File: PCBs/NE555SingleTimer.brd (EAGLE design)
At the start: 24.2 x 19 mm, 7 parts, among them T1 2N3904

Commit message: Renamed files .
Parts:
- removed GND, INPUT, OUTPUT: MICROBIT_PAD, microbit:MICROBIT_PAD
- removed LED1: (no value), led:CHIP-LED0805
- removed R1, R2: (no value), we-rcl:R0207/10
- removed T1: 2N3904, transistor:TO92
- added IC1: LM555N, linear:DIL08
- added U$1, U$2, U$3, U$4: MICROBIT_PAD, microbit:MICROBIT_PAD
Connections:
- removed net N$3: R1.2, T1.2
- net 5V: now also IC1.4, IC1.8, U$3.PAD; no longer INPUT.PAD, R1.1, R2.2
- net GND: now also IC1.1, U$4.PAD; no longer GND.PAD, T1.3
- net N$1: now also IC1.3, U$1.PAD; no longer LED1.A, R2.1
- net N$2: now also IC1.2, IC1.6, U$2.PAD; no longer LED1.C, OUTPUT.PAD, T1.1
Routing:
- net N$1: track 1.95 -> 13.8 mm
- net 5V: track 10.3 -> 20.4 mm
- net N$3: track 6.06 -> 0.00 mm
- net GND: track 10.3 -> 5.17 mm
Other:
- board size 24.2 x 19 mm -> 16.5 x 31.8 mm
- board text added: "555IC"

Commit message: Updated
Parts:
- moved U$1 0.30 mm to (12.0, 25.0)
- moved U$2 0.13 mm to (4.32, 24.9)
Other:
- board size 16.5 x 31.8 mm -> 22.5 x 32 mm
- board text added: "PinwheelRobotics"
- board text added: "care@pinwheel"
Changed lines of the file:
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@@
 <drawing>
 <settings>
-<setting alwaysvectorfont="no"/>
+<setting alwaysvectorfont="yes"/>
 <setting verticaltext="up"/>
 </settings>
-<grid distance="50" unitdist="mil" unit="mm" style="lines" multiple="1" display="yes" altdistance="5" altunitdist="mil" altunit="mm"/>
+<grid distance="0.5" unitdist="mm" unit="mm" style="lines" multiple="1" display="yes" altdistance="5" altunitdist="mil" altunit="mm"/>
 <layers>
 <layer number="1" name="Top" color="4" fill="1" visible="yes" active="yes"/>
@@
 <layer number="43" name="vRestrict" color="2" fill="10" visible="yes" active="yes"/>
 <layer number="44" name="Drills" color="7" fill="1" visible="no" active="yes"/>
-<layer number="45" name="Holes" color="7" fill="1" visible="no" active="yes"/>
+<layer number="45" name="Holes" color="7" fill="1" visible="yes" active="yes"/>
 <layer number="46" name="Milling" color="3" fill="1" visible="no" active="yes"/>
 <layer number="47" name="Measures" color="7" fill="1" visible="no" active="yes"/>
@@
 <plain>
 <text x="15.113" y="15.621" size="0.4064" layer="21" rot="R90">555IC</text>
-<wire x1="1.27" y1="0" x2="15.24" y2="0" width="0.1524" layer="20"/>
-<wire x1="15.24" y1="0" x2="16.51" y2="1.27" width="0.1524" layer="20" curve="90"/>
-<wire x1="16.51" y1="1.27" x2="16.51" y2="30.48" width="0.1524" layer="20"/>
-<wire x1="16.51" y1="30.48" x2="15.24" y2="31.75" width="0.1524" layer="20" curve="90"/>
-<wire x1="15.24" y1="31.75" x2="1.27" y2="31.75" width="0.1524" layer="20"/>
-<wire x1="1.27" y1="31.75" x2="0" y2="30.48" width="0.1524" layer="20" curve="90"/>
-<wire x1="0" y1="30.48" x2="0" y2="1.27" width="0.1524" layer="20"/>
-<wire x1="0" y1="1.27" x2="1.27" y2="0" width="0.1524" layer="20" curve="90"/>
+<wire x1="-3" y1="30.788903125" x2="-3" y2="0.998303125" width="0.1524" layer="20"/>
+<wire x1="-3" y1="0.998303125" x2="-2.001696875" y2="0" width="0.1524" layer="20" curve="90"/>
+<wire x1="-2.001696875" y1="0" x2="17.86581875" y2="0" width="0.1524" layer="20"/>
+<wire x1="17.86581875" y1="0" x2="19.5" y2="1.63418125" width="0.1524" layer="20" curve="90"/>
+<wire x1="19.5" y1="1.63418125" x2="19.5" y2="30.165390625" width="0.1524" layer="20"/>
+<wire x1="19.5" y1="30.165390625" x2="17.665390625" y2="32" width="0.1524" layer="20" curve="90"/>
+<wire x1="17.665390625" y1="32" x2="-1.788903125" y2="32" width="0.1524" layer="20"/>
+<wire x1="-1.788903125" y1="32" x2="-3" y2="30.788903125" width="0.1524" layer="20" curve="90"/>
+<hole x="-1" y="30" drill="3"/>
+<hole x="17.5" y="29.881" drill="3"/>
+<hole x="17.5" y="2" drill="3"/>
+<hole x="-1" y="2" drill="3"/>
+<text x="0" y="6" size="1.778" layer="21" rot="R90">PinwheelRobotics </text>
+<text x="18.5" y="25" size="1.778" layer="22" rot="MR270">care@pinwheel</text>
 </plain>
 <attributes>
@@
 <attribute name="VALUE" x="5.207" y="15.24" size="1.27" layer="27" ratio="10"/>
 </element>
-<element name="U$1" library="microbit" package="MICROBIT_PAD" value="MICROBIT_PAD" x="12.192" y="24.765" smashed="yes" rot="R180">
-<attribute name="NAME" x="15.367" y="19.685" size="1.27" layer="21" rot="R90"/>
+<element name="U$1" library="microbit" package="MICROBIT_PAD" value="MICROBIT_PAD" x="12" y="25" smashed="yes" rot="R180">
+<attribute name="NAME" x="15.175" y="19.92" size="1.27" layer="21" rot="R90"/>
 </element>
-<element name="U$2" library="microbit" package="MICROBIT_PAD" value="MICROBIT_PAD" x="4.318" y="24.765" smashed="yes" rot="R180">
-<attribute name="NAME" x="1.016" y="20.447" size="1.27" layer="21"/>
+<element name="U$2" library="microbit" package="MICROBIT_PAD" value="MICROBIT_PAD" x="4.318" y="24.892" smashed="yes" rot="R180">
+<attribute name="NAME" x="1.016" y="20.574" size="1.27" layer="21"/>
 </element>
 <element name="U$3" library="microbit" package="MICROBIT_PAD" value="MICROBIT_PAD" x="12.192" y="6.985" smashed="yes">
@@
 <wire x1="11.2268" y1="19.1516" x2="10.2362" y2="18.161" width="0.508" layer="16"/>
 <wire x1="11.2268" y1="24.1046" x2="11.2268" y2="19.1516" width="0.508" layer="16"/>
-<wire x1="11.8872" y1="24.765" x2="11.2268" y2="24.1046" width="0.508" layer="16"/>
+<wire x1="12" y1="24.8778" x2="11.2268" y2="24.1046" width="0.508" layer="16"/>
 <wire x1="10.2362" y1="12.2174" x2="10.033" y2="12.065" width="0.508" layer="16"/>
-<wire x1="11.8872" y1="24.765" x2="12.192" y2="24.765" width="0.508" layer="16"/>
+<wire x1="12" y1="24.8778" x2="12" y2="25" width="0.508" layer="16"/>
 </signal>
 <signal name="N$2">
@@
 <wire x1="7.5946" y1="12.2174" x2="7.493" y2="12.065" width="0.508" layer="16"/>
 <wire x1="9.906" y1="19.4818" x2="10.033" y2="19.685" width="0.508" layer="16"/>
-<wire x1="4.953" y1="24.765" x2="10.033" y2="19.685" width="0.508" layer="16"/>
-<wire x1="4.318" y1="24.765" x2="4.953" y2="24.765" width="0.508" layer="16"/>
+<wire x1="4.826" y1="24.892" x2="10.033" y2="19.685" width="0.508" layer="16"/>
+<wire x1="4.318" y1="24.892" x2="4.826" y2="24.892" width="0.508" layer="16"/>
 </signal>
 <signal name="GND">

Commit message: New Update
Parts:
- moved U$3 0.40 mm to (11.8, 7.11)
- moved U$1 0.25 mm to (11.7, 25.0)
- moved U$4 0.13 mm to (4.32, 7.11)
- moved U$2 0.13 mm to (4.32, 25.0)
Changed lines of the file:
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@@
 <drawing>
 <settings>
-<setting alwaysvectorfont="yes"/>
+<setting alwaysvectorfont="no"/>
 <setting verticaltext="up"/>
 </settings>
@@
 <wire x1="-1.788903125" y1="32" x2="-3" y2="30.788903125" width="0.1524" layer="20" curve="90"/>
 <hole x="-1" y="30" drill="3"/>
-<hole x="17.5" y="29.881" drill="3"/>
-<hole x="17.5" y="2" drill="3"/>
+<hole x="17" y="30" drill="3"/>
+<hole x="17" y="2" drill="3"/>
 <hole x="-1" y="2" drill="3"/>
 <text x="0" y="6" size="1.778" layer="21" rot="R90">PinwheelRobotics </text>
@@
 <attribute name="VALUE" x="5.207" y="15.24" size="1.27" layer="27" ratio="10"/>
 </element>
-<element name="U$1" library="microbit" package="MICROBIT_PAD" value="MICROBIT_PAD" x="12" y="25" smashed="yes" rot="R180">
-<attribute name="NAME" x="15.175" y="19.92" size="1.27" layer="21" rot="R90"/>
+<element name="U$1" library="microbit" package="MICROBIT_PAD" value="MICROBIT_PAD" x="11.746" y="25" smashed="yes" rot="R180">
+<attribute name="NAME" x="14.921" y="19.92" size="1.27" layer="21" rot="R90"/>
 </element>
-<element name="U$2" library="microbit" package="MICROBIT_PAD" value="MICROBIT_PAD" x="4.318" y="24.892" smashed="yes" rot="R180">
-<attribute name="NAME" x="1.016" y="20.574" size="1.27" layer="21"/>
+<element name="U$2" library="microbit" package="MICROBIT_PAD" value="MICROBIT_PAD" x="4.318" y="25.019" smashed="yes" rot="R180">
+<attribute name="NAME" x="1.016" y="20.701" size="1.27" layer="21"/>
 </element>
-<element name="U$3" library="microbit" package="MICROBIT_PAD" value="MICROBIT_PAD" x="12.192" y="6.985" smashed="yes">
-<attribute name="NAME" x="14.097" y="11.176" size="1.27" layer="21" rot="R270"/>
+<element name="U$3" library="microbit" package="MICROBIT_PAD" value="MICROBIT_PAD" x="11.811" y="7.112" smashed="yes">
+<attribute name="NAME" x="13.716" y="11.303" size="1.27" layer="21" rot="R270"/>
 </element>
-<element name="U$4" library="microbit" package="MICROBIT_PAD" value="MICROBIT_PAD" x="4.445" y="7.112" smashed="yes">
-<attribute name="NAME" x="1.143" y="12.319" size="1.27" layer="21" rot="R270"/>
+<element name="U$4" library="microbit" package="MICROBIT_PAD" value="MICROBIT_PAD" x="4.318" y="7.112" smashed="yes">
+<attribute name="NAME" x="1.016" y="12.319" size="1.27" layer="21" rot="R270"/>
 </element>
 </elements>
@@
 <wire x1="12.5476" y1="7.5946" x2="12.5476" y2="10.8966" width="0.508" layer="16"/>
 <wire x1="12.5476" y1="10.8966" x2="12.5476" y2="11.8872" width="0.508" layer="16"/>
-<wire x1="12.2428" y1="7.2898" x2="12.5476" y2="7.5946" width="0.508" layer="16"/>
+<wire x1="12.1158" y1="7.1628" x2="12.5476" y2="7.5946" width="0.508" layer="16"/>
 <wire x1="12.5476" y1="11.8872" x2="12.573" y2="12.065" width="0.508" layer="16"/>
-<wire x1="12.2428" y1="7.2898" x2="12.192" y2="6.985" width="0.508" layer="16"/>
+<wire x1="12.1158" y1="7.1628" x2="11.811" y2="7.112" width="0.508" layer="16"/>
 <wire x1="4.953" y1="13.8684" x2="4.953" y2="19.685" width="0.508" layer="16"/>
 <wire x1="6.2738" y1="12.5476" x2="4.953" y2="13.8684" width="0.508" layer="16"/>
@@
 <wire x1="11.2268" y1="19.1516" x2="10.2362" y2="18.161" width="0.508" layer="16"/>
 <wire x1="11.2268" y1="24.1046" x2="11.2268" y2="19.1516" width="0.508" layer="16"/>
-<wire x1="12" y1="24.8778" x2="11.2268" y2="24.1046" width="0.508" layer="16"/>
+<wire x1="11.746" y1="24.6238" x2="11.2268" y2="24.1046" width="0.508" layer="16"/>
 <wire x1="10.2362" y1="12.2174" x2="10.033" y2="12.065" width="0.508" layer="16"/>
-<wire x1="12" y1="24.8778" x2="12" y2="25" width="0.508" layer="16"/>
+<wire x1="11.746" y1="24.6238" x2="11.746" y2="25" width="0.508" layer="16"/>
 </signal>
 <signal name="N$2">
@@
 <wire x1="7.5946" y1="12.2174" x2="7.493" y2="12.065" width="0.508" layer="16"/>
 <wire x1="9.906" y1="19.4818" x2="10.033" y2="19.685" width="0.508" layer="16"/>
-<wire x1="4.826" y1="24.892" x2="10.033" y2="19.685" width="0.508" layer="16"/>
-<wire x1="4.318" y1="24.892" x2="4.826" y2="24.892" width="0.508" layer="16"/>
+<wire x1="4.699" y1="25.019" x2="10.033" y2="19.685" width="0.508" layer="16"/>
+<wire x1="4.318" y1="25.019" x2="4.699" y2="25.019" width="0.508" layer="16"/>
 </signal>
 <signal name="GND">
 <contactref element="IC1" pad="1"/>
 <contactref element="U$4" pad="PAD"/>
-<wire x1="4.953" y1="7.5946" x2="4.953" y2="12.065" width="0.508" layer="16"/>
-<wire x1="4.6228" y1="7.2644" x2="4.953" y2="7.5946" width="0.508" layer="16"/>
-<wire x1="4.6228" y1="7.2644" x2="4.445" y2="7.112" width="0.508" layer="16"/>
+<wire x1="4.953" y1="7.656284375" x2="4.953" y2="12.065" width="0.508" layer="16"/>
+<wire x1="4.953" y1="7.656284375" x2="4.318" y2="7.112" width="0.508" layer="16"/>
 </signal>
 </signals>

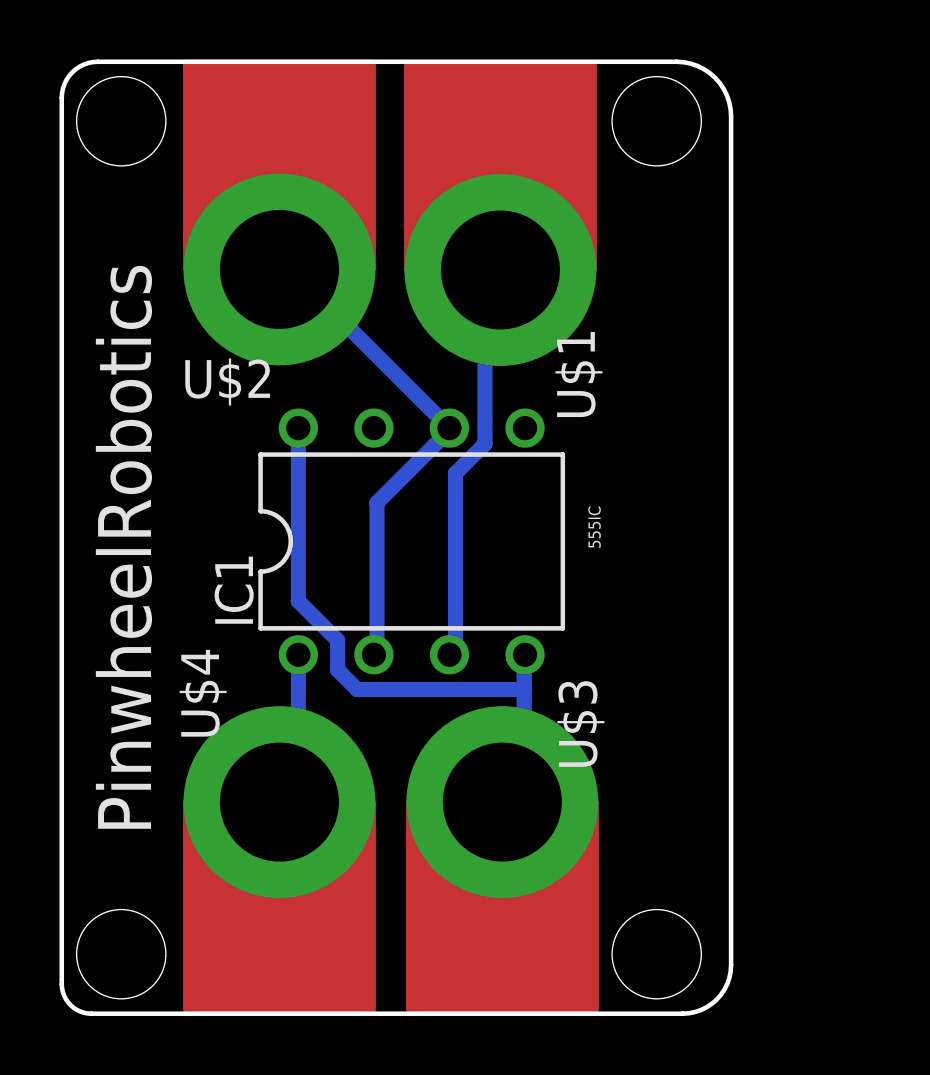
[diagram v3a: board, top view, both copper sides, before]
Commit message: New Update for board curv
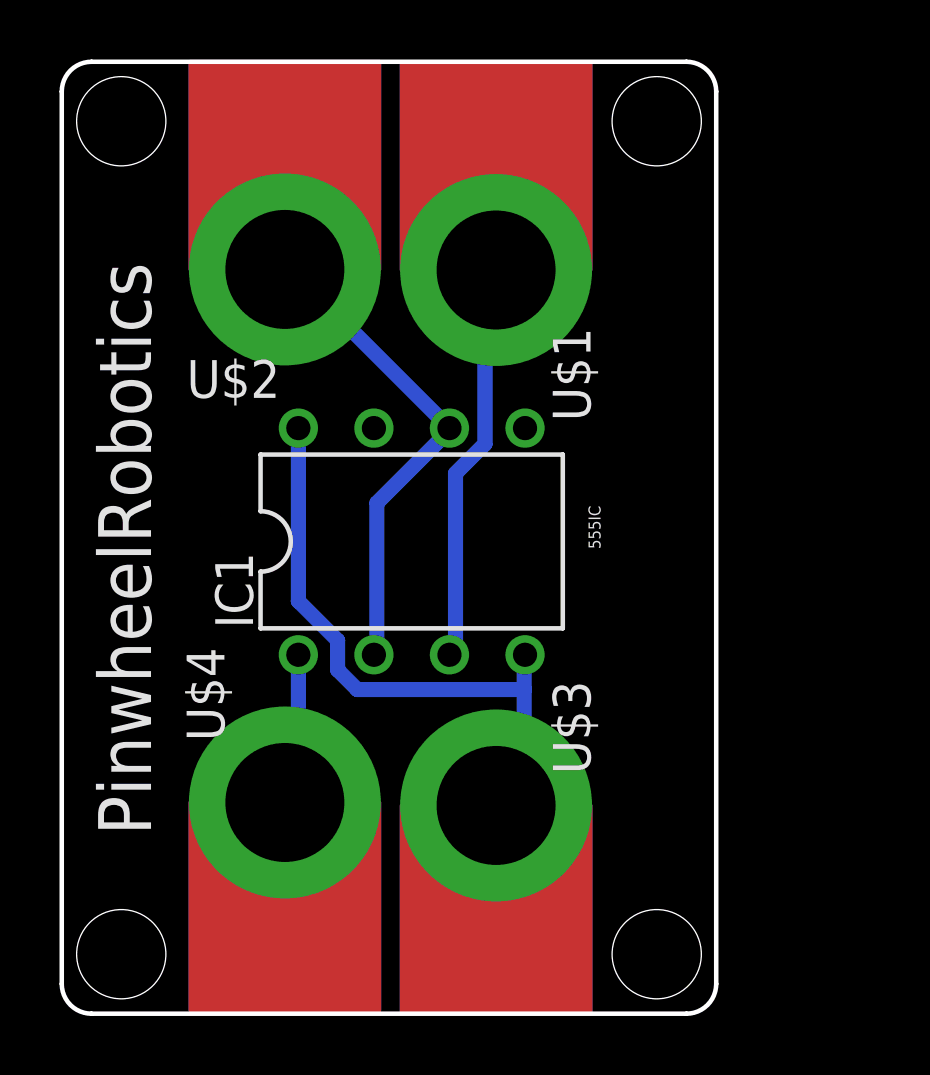
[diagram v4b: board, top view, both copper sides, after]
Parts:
- moved U$3 0.24 mm to (11.6, 7.00)
- moved U$4 0.18 mm to (4.50, 7.10)
- moved U$2 0.18 mm to (4.50, 25.0)
- moved U$1 0.15 mm to (11.6, 25.0)
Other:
- board size 22.5 x 32 mm -> 22 x 32 mm
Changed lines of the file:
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@@
 <drawing>
 <settings>
-<setting alwaysvectorfont="no"/>
+<setting alwaysvectorfont="yes"/>
 <setting verticaltext="up"/>
 </settings>
@@
 <plain>
 <text x="15.113" y="15.621" size="0.4064" layer="21" rot="R90">555IC</text>
-<wire x1="-3" y1="30.788903125" x2="-3" y2="0.998303125" width="0.1524" layer="20"/>
-<wire x1="-3" y1="0.998303125" x2="-2.001696875" y2="0" width="0.1524" layer="20" curve="90"/>
-<wire x1="-2.001696875" y1="0" x2="17.86581875" y2="0" width="0.1524" layer="20"/>
-<wire x1="17.86581875" y1="0" x2="19.5" y2="1.63418125" width="0.1524" layer="20" curve="90"/>
-<wire x1="19.5" y1="1.63418125" x2="19.5" y2="30.165390625" width="0.1524" layer="20"/>
-<wire x1="19.5" y1="30.165390625" x2="17.665390625" y2="32" width="0.1524" layer="20" curve="90"/>
-<wire x1="17.665390625" y1="32" x2="-1.788903125" y2="32" width="0.1524" layer="20"/>
-<wire x1="-1.788903125" y1="32" x2="-3" y2="30.788903125" width="0.1524" layer="20" curve="90"/>
+<wire x1="18" y1="32" x2="-2" y2="32" width="0.1524" layer="20"/>
+<wire x1="-2" y1="32" x2="-3" y2="31" width="0.1524" layer="20" curve="90"/>
+<wire x1="-3" y1="31" x2="-3" y2="1" width="0.1524" layer="20"/>
+<wire x1="-3" y1="1" x2="-2" y2="0" width="0.1524" layer="20" curve="90"/>
+<wire x1="-2" y1="0" x2="18" y2="0" width="0.1524" layer="20"/>
+<wire x1="18" y1="0" x2="19" y2="1" width="0.1524" layer="20" curve="90"/>
+<wire x1="19" y1="1" x2="19" y2="31" width="0.1524" layer="20"/>
+<wire x1="19" y1="31" x2="18" y2="32" width="0.1524" layer="20" curve="90"/>
 <hole x="-1" y="30" drill="3"/>
 <hole x="17" y="30" drill="3"/>
@@
 <attribute name="VALUE" x="5.207" y="15.24" size="1.27" layer="27" ratio="10"/>
 </element>
-<element name="U$1" library="microbit" package="MICROBIT_PAD" value="MICROBIT_PAD" x="11.746" y="25" smashed="yes" rot="R180">
-<attribute name="NAME" x="14.921" y="19.92" size="1.27" layer="21" rot="R90"/>
+<element name="U$1" library="microbit" package="MICROBIT_PAD" value="MICROBIT_PAD" x="11.6" y="25" smashed="yes" rot="R180">
+<attribute name="NAME" x="14.775" y="19.92" size="1.27" layer="21" rot="R90"/>
 </element>
-<element name="U$2" library="microbit" package="MICROBIT_PAD" value="MICROBIT_PAD" x="4.318" y="25.019" smashed="yes" rot="R180">
-<attribute name="NAME" x="1.016" y="20.701" size="1.27" layer="21"/>
+<element name="U$2" library="microbit" package="MICROBIT_PAD" value="MICROBIT_PAD" x="4.5" y="25.019" smashed="yes" rot="R180">
+<attribute name="NAME" x="1.198" y="20.701" size="1.27" layer="21"/>
 </element>
-<element name="U$3" library="microbit" package="MICROBIT_PAD" value="MICROBIT_PAD" x="11.811" y="7.112" smashed="yes">
-<attribute name="NAME" x="13.716" y="11.303" size="1.27" layer="21" rot="R270"/>
+<element name="U$3" library="microbit" package="MICROBIT_PAD" value="MICROBIT_PAD" x="11.6" y="7" smashed="yes">
+<attribute name="NAME" x="13.505" y="11.191" size="1.27" layer="21" rot="R270"/>
 </element>
-<element name="U$4" library="microbit" package="MICROBIT_PAD" value="MICROBIT_PAD" x="4.318" y="7.112" smashed="yes">
-<attribute name="NAME" x="1.016" y="12.319" size="1.27" layer="21" rot="R270"/>
+<element name="U$4" library="microbit" package="MICROBIT_PAD" value="MICROBIT_PAD" x="4.5" y="7.1" smashed="yes">
+<attribute name="NAME" x="1.198" y="12.307" size="1.27" layer="21" rot="R270"/>
 </element>
 </elements>
@@
 <wire x1="12.1158" y1="7.1628" x2="12.5476" y2="7.5946" width="0.508" layer="16"/>
 <wire x1="12.5476" y1="11.8872" x2="12.573" y2="12.065" width="0.508" layer="16"/>
-<wire x1="12.1158" y1="7.1628" x2="11.811" y2="7.112" width="0.508" layer="16"/>
+<wire x1="12.1158" y1="7.1628" x2="11.6" y2="7" width="0.508" layer="16"/>
 <wire x1="4.953" y1="13.8684" x2="4.953" y2="19.685" width="0.508" layer="16"/>
 <wire x1="6.2738" y1="12.5476" x2="4.953" y2="13.8684" width="0.508" layer="16"/>
@@
 <wire x1="11.746" y1="24.6238" x2="11.2268" y2="24.1046" width="0.508" layer="16"/>
 <wire x1="10.2362" y1="12.2174" x2="10.033" y2="12.065" width="0.508" layer="16"/>
-<wire x1="11.746" y1="24.6238" x2="11.746" y2="25" width="0.508" layer="16"/>
+<wire x1="11.746" y1="24.6238" x2="11.6" y2="25" width="0.508" layer="16"/>
 </signal>
 <signal name="N$2">
@@
 <wire x1="9.906" y1="19.4818" x2="10.033" y2="19.685" width="0.508" layer="16"/>
 <wire x1="4.699" y1="25.019" x2="10.033" y2="19.685" width="0.508" layer="16"/>
-<wire x1="4.318" y1="25.019" x2="4.699" y2="25.019" width="0.508" layer="16"/>
+<wire x1="4.5" y1="25.019" x2="4.699" y2="25.019" width="0.508" layer="16"/>
 </signal>
 <signal name="GND">
@@
 <contactref element="U$4" pad="PAD"/>
 <wire x1="4.953" y1="7.656284375" x2="4.953" y2="12.065" width="0.508" layer="16"/>
-<wire x1="4.953" y1="7.656284375" x2="4.318" y2="7.112" width="0.508" layer="16"/>
+<wire x1="4.953" y1="7.656284375" x2="4.5" y2="7.1" width="0.508" layer="16"/>
 </signal>
 </signals>
